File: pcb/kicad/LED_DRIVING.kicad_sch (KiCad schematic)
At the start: 43 parts, among them Q1 DMP3125L-7, Q2 DMP3125L-7, Q3 DMP3125L-7, Q4 DMP3125L-7, Q5 DMP3125L-7, Q6 DMP3125L-7, Q7 DMP3125L-7, Q8 DMP3125L-7, U3 STP16CP05XT, U4 STP16CP05XT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

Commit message: Update parts/mpns/descriptions etc.
- Incorrect LED part, was 0805 package instead of 0603
- Added MPNs for other parts (mostly ones I already own multiples of)
- Update schematics?
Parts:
- R10, R11, R12, R5, R6, R7, R8, R9: MPN (none) -> RT0603FRE0710RL
- R13, R14, R15, R16, R17, R18, R19, R20, R29, R30, R31: MPN (none) -> RT0603DRE071KL
- R21, R22, R23, R24, R25, R26, R27, R28: MPN (none) -> RT0603FRE075K1L
- RV1: MPN (none) -> 3386F-1-222LF

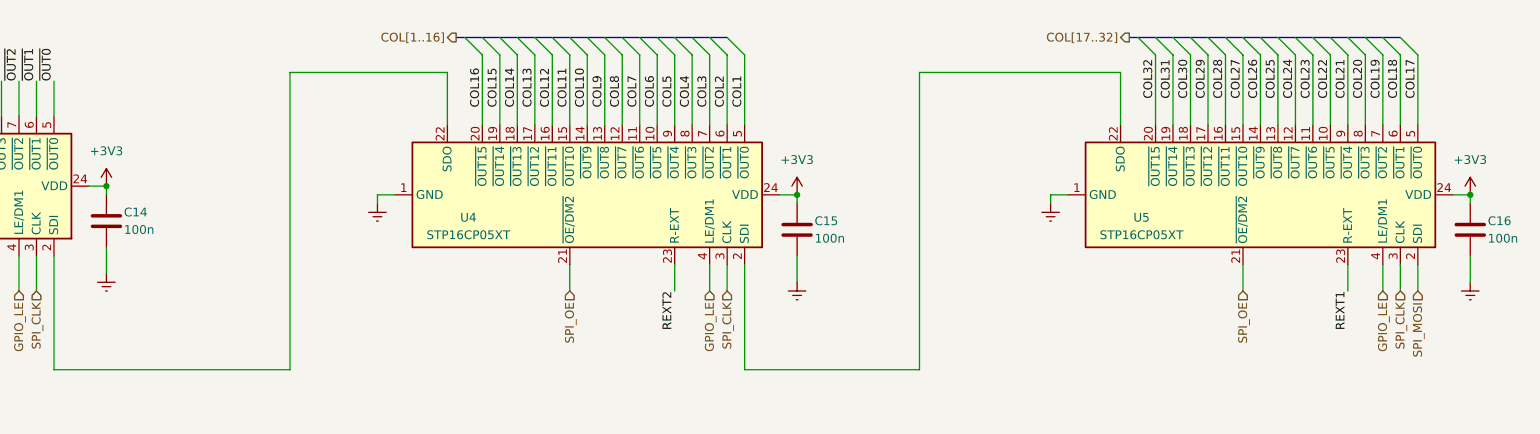
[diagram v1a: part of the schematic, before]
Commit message: Update capcitor annotations
- One less capacitor therefore the symbol annotations need to be changed
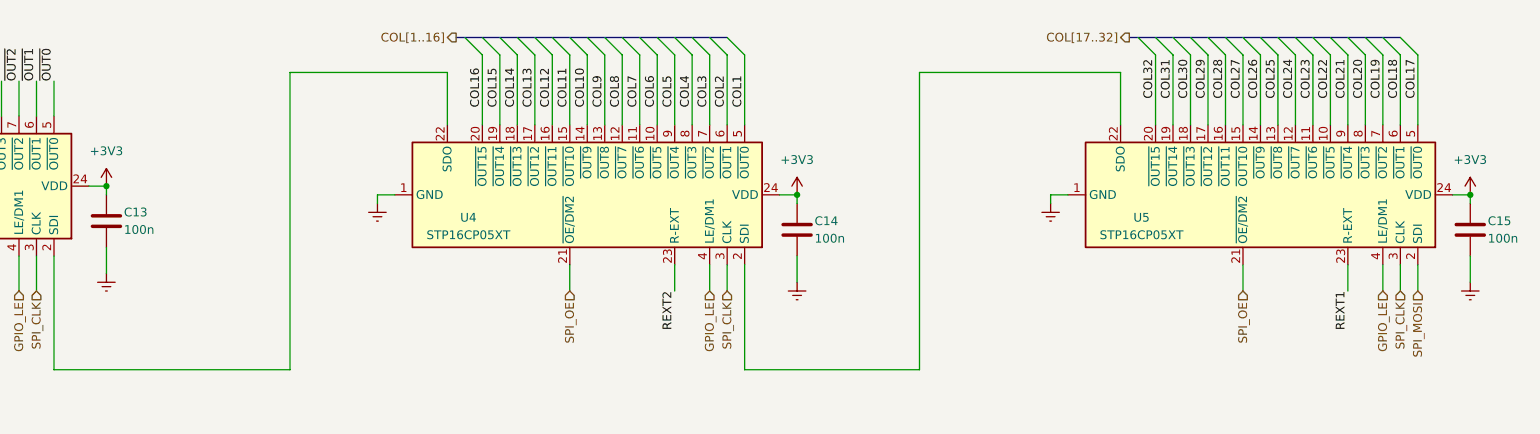
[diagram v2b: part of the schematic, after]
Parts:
- renumbered C14 to C13, C15 to C14, C16 to C15
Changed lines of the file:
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@@
 	(title_block
 		(title "8x32 LED Matrix")
-		(date "2024-11-24")
-		(rev "v03")
+		(date "2025-05-21")
+		(rev "v04")
 		(comment 4 "STP16CP05 based cascaded LED matrices")
 	)
@@
 		(on_board yes)
 		(dnp no)
-		(property "Reference" "C16"
+		(property "Reference" "C15"
 			(at 345.44 77.47 0)
 			(effects
@@
 			(project "i2s_spekky_matrix"
 				(path "/e164be4c-4870-49b4-a08f-d162a756edc1/4cb753b0-d3ca-49e3-8f9f-0ad77b1cdcd0"
-					(reference "C16")
+					(reference "C15")
 					(unit 1)
 				)
@@
 		(on_board yes)
 		(dnp no)
-		(property "Reference" "C14"
+		(property "Reference" "C13"
 			(at 147.32 76.2 0)
 			(effects
@@
 			(project "i2s_spekky_matrix"
 				(path "/e164be4c-4870-49b4-a08f-d162a756edc1/4cb753b0-d3ca-49e3-8f9f-0ad77b1cdcd0"
-					(reference "C14")
+					(reference "C13")
 					(unit 1)
 				)
@@
 		(on_board yes)
 		(dnp no)
-		(property "Reference" "C15"
+		(property "Reference" "C14"
 			(at 247.65 77.47 0)
 			(effects
@@
 			(project "i2s_spekky_matrix"
 				(path "/e164be4c-4870-49b4-a08f-d162a756edc1/4cb753b0-d3ca-49e3-8f9f-0ad77b1cdcd0"
-					(reference "C15")
+					(reference "C14")
 					(unit 1)
 				)

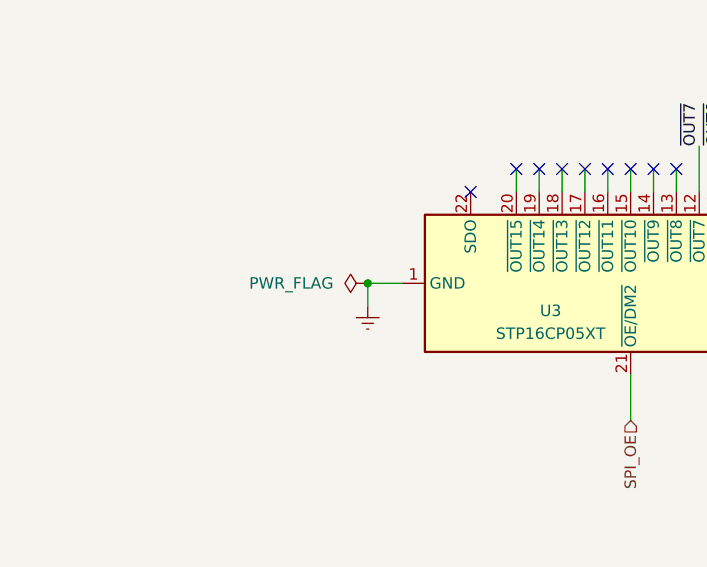
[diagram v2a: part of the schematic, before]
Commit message: Update gndref net to gnd
- Changes applied to schematic and PCB
- Using GNDREF symbol for GND but need to change the net name
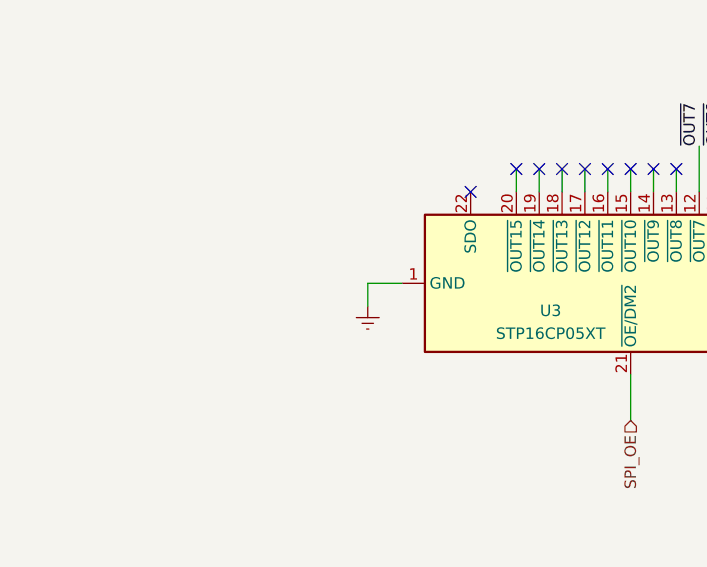
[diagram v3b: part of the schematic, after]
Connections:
- net GNDREF renamed GND
